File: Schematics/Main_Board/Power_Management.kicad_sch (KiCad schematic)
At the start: 6 parts

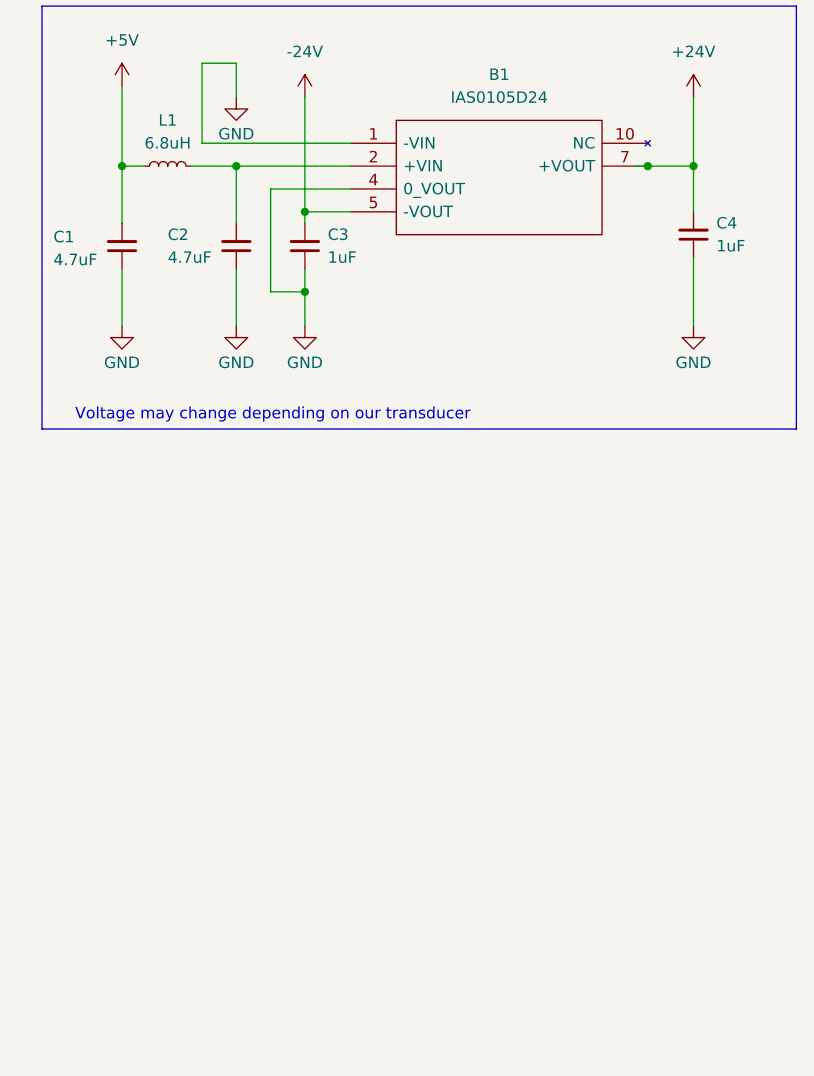
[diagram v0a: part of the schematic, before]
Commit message: organizational changes to schematic
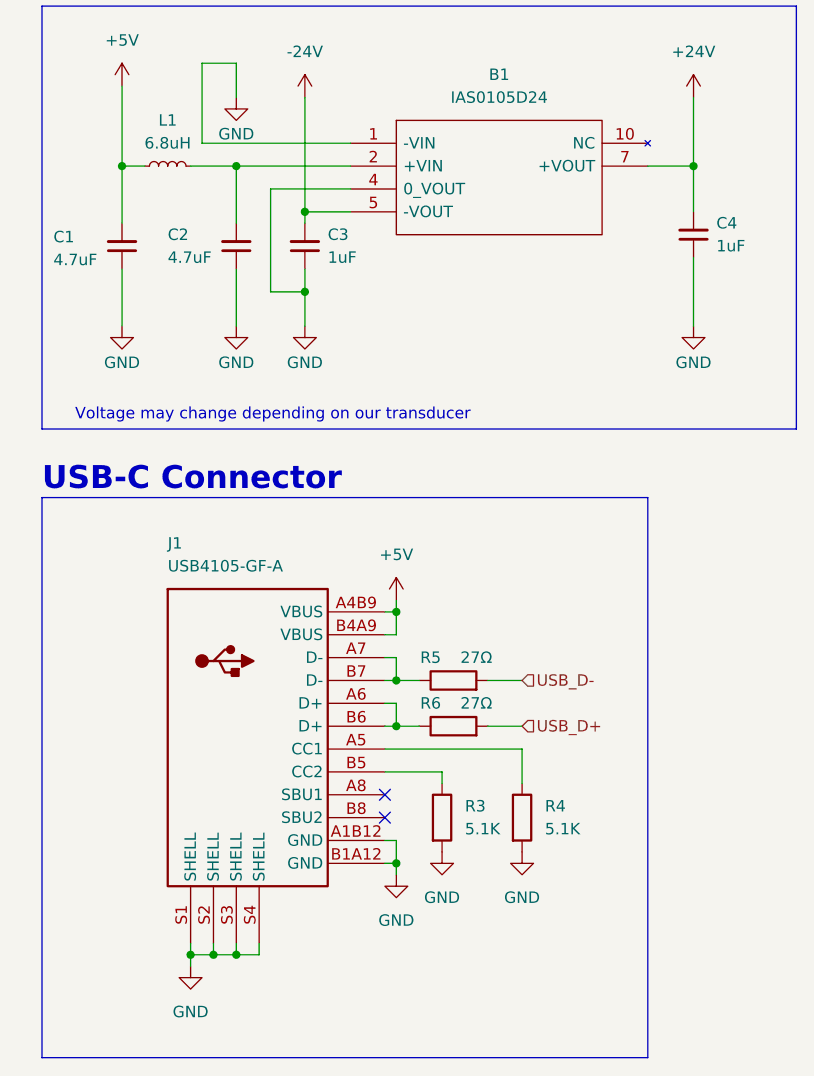
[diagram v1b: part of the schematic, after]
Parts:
- added J1: USB4105-GF-A, Eclectronics:USB4105-GF-A, symbol Eclectronics:USB4105-GF-A
- added R3, R4: 5.1K, Resistor_SMD:R_0402_1005Metric, symbol Device:R
- added R5, R6: 27Ω, Resistor_SMD:R_0402_1005Metric, symbol Device:R
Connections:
- net +5V: now also J1.A4B9 (VBUS), J1.B4A9 (VBUS)
- net GND: now also J1.A1B12 (GND), J1.B1A12 (GND), J1.S1 (SHELL), J1.S2 (SHELL), J1.S3 (SHELL), J1.S4 (SHELL), R3.2, R4.2
- new net: J1.A5 (CC1), R4.1
- new net: J1.A6 (D+), J1.B6 (D+), R6.1
- new net: J1.A7 (D-), J1.B7 (D-), R5.1
- new net: J1.B5 (CC2), R3.1
- new net USB_D+: R6.2
- new net USB_D-: R5.2
- no-connect marks 0 -> 2
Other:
- note added: "USB-C Connector"

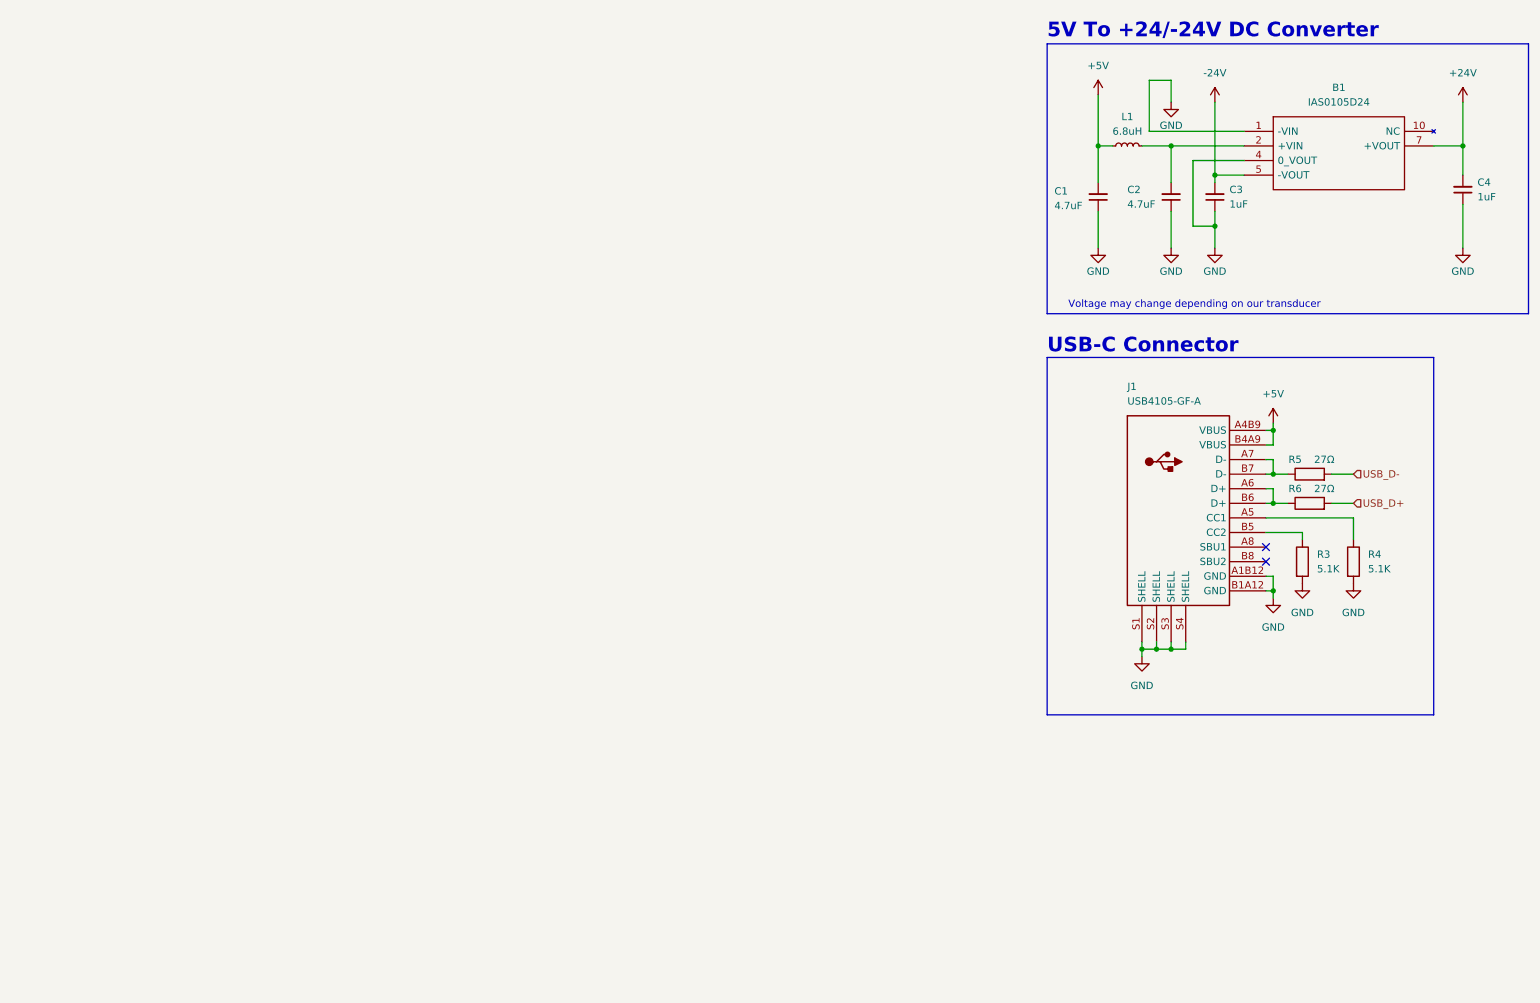
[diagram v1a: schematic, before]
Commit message: Added initial Lipo Charger and BMS, reorganized footprint library and merged symbol libraries
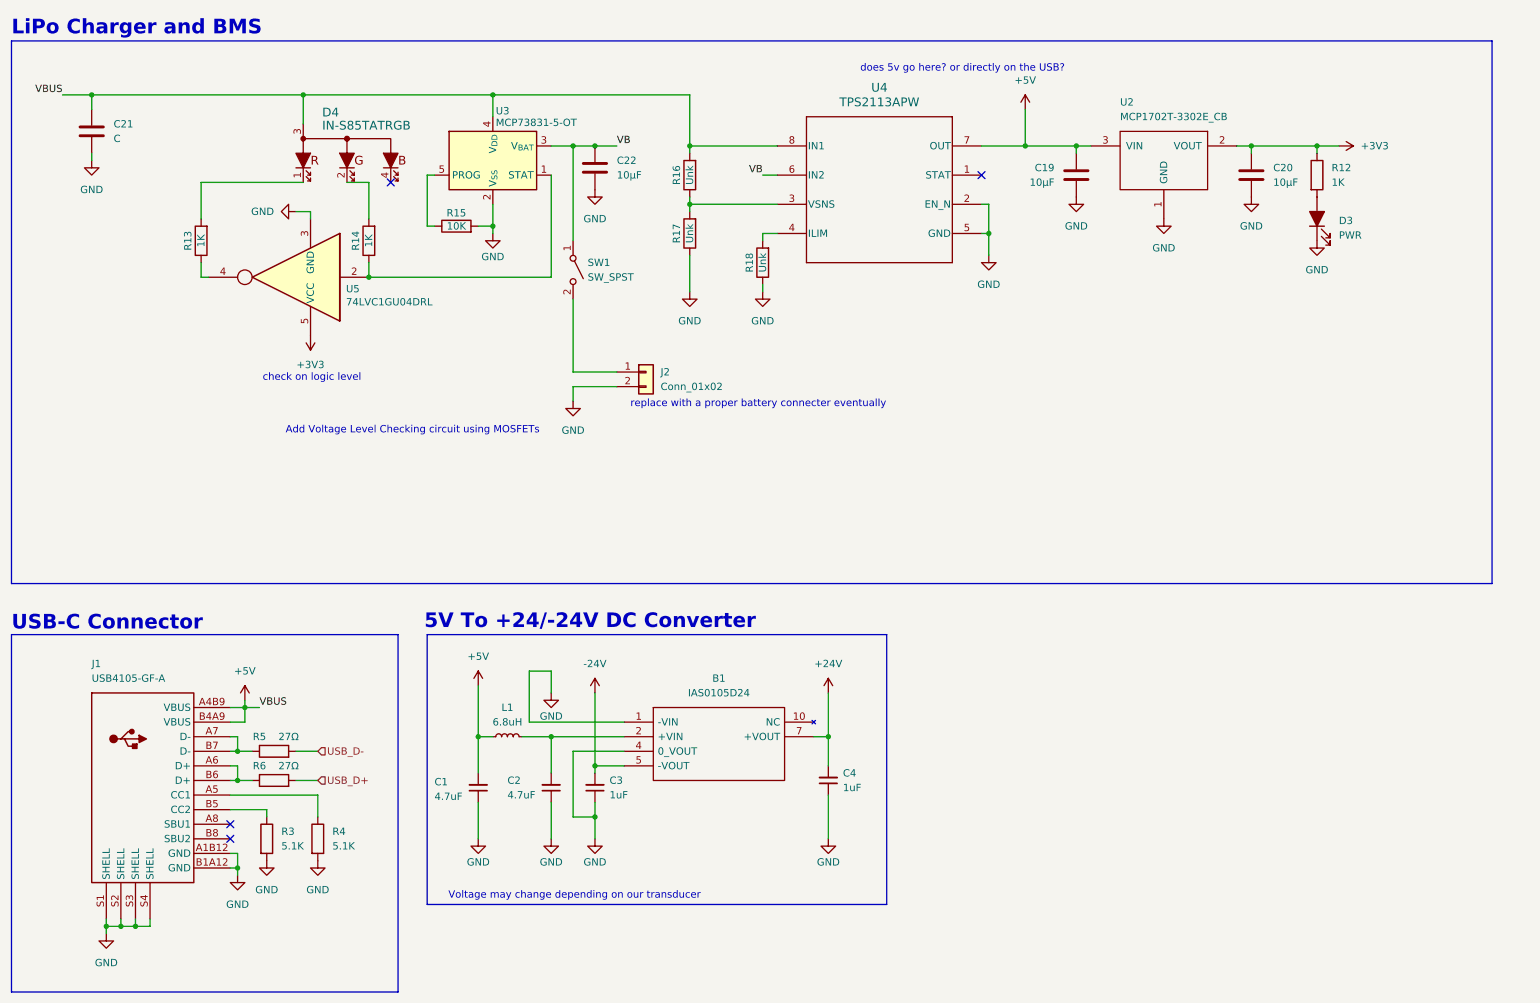
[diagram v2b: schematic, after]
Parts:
- added C19, C20, C22: 10µF, Capacitor_SMD:C_0603_1608Metric, symbol Device:C
- added C21: C, symbol Device:C
- added D3: PWR, LED_SMD:LED_0805_2012Metric, symbol Device:LED_Filled
- added D4: IN-S85TATRGB, PU_Lib:IN-S85TATRGB, symbol PU_Lib:IN-S85TATRGB
- added J2: Conn_01x02, symbol Connector_Generic:Conn_01x02
- added R12: 1K, Resistor_SMD:R_0402_1005Metric, symbol Device:R
- added R13, R14: 1K, symbol Device:R
- added R15: 10K, symbol Device:R
- added R16, R17, R18: Unk, symbol Device:R
- added SW1: SW_SPST, symbol Switch:SW_SPST
- added U2: MCP1702T-3302E_CB, PU_Lib:SOT-23A_MC_MCH, symbol PU_Lib:MCP1702T-3302E_CB
- added U3: MCP73831-5-OT, Package_TO_SOT_SMD:SOT-23-5, symbol Battery_Management:MCP73831-5-OT
- added U4: TPS2113APW, PU_Lib:TPS2113APW_N, symbol PU_Lib:TPS2113APW
- added U5: 74LVC1GU04DRL, Package_TO_SOT_SMD:SOT-553, symbol 74xGxx:74LVC1GU04DRL
- B1: symbol PMOD_PULSER:IAS0105D24 -> PU_Lib:IAS0105D24
- J1: footprint Eclectronics:USB4105-GF-A -> PU_Lib:USB4105-GF-A; symbol Eclectronics:USB4105-GF-A -> PU_Lib:USB4105-GF-A
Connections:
- net +5V: now also C19.2, C21.1, D4.3, R16.2, U2.3 (VIN), U3.4 (V_{DD}), U4.7 (OUT), U4.8 (IN1)
- net GND: now also C19.1, C20.2, C21.2, C22.2, D3.1 (K), J2.2 (Pin_2), R15.2, R17.1, R18.1, U2.1 (GND), U3.2 (V_{SS}), U4.2 (EN_N), U4.5 (GND), U5.3 (GND)
- new net: R14.1, U3.1 (STAT), U5.2
- new net: R13.1, U5.4
- new net: D4.1, R13.2
- new net: D4.2, R14.2
- new net: D3.2 (A), R12.2
- new net: J2.1 (Pin_1), SW1.2 (B)
- new net: R18.2, U4.4 (ILIM)
- new net: R16.1, R17.2, U4.3 (VSNS)
- new net: R15.1, U3.5 (PROG)
- new net +3V3: C20.1, R12.1, U2.2 (VOUT), U5.5 (VCC)
- new net VB: C22.1, SW1.1 (A), U3.3 (V_{BAT}), U4.6 (IN2)
- no-connect marks 2 -> 4
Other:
- note added: "Add Voltage Level Checking circuit using MOSFETs"
- note added: "LiPo Charger and BMS"
- note added: "check on logic level"
- note added: "does 5v go here? or directly on the USB?"
- note added: "replace with a proper battery connecter eventually"
- moved on the sheet: B1, C1, C2, C3, C4, J1, L1, R3, R4, R5, R6
